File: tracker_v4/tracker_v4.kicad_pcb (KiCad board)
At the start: 2 copper layers, 62.5 x 22.1 mm, 36 parts, among them J1 USB_C_Receptacle_PowerOnly_6P, J2 P70-7000045, J3 P70-7000045, Q1 DMG9926UDM-7, U1 XIAO-ESP32-DIP, U2 LIS3DH, U3 DW01A, U4 INA226AIDGSR, U5 TP4056-42-ESOP8

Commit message: started pcb v4
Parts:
- removed J2, J3: P70-7000045, P70_7000045:HARWIN_P70-7000045
- added C4: 1u, Capacitor_SMD:C_0603_1608Metric, F.Cu at (146.0, 81.3)
- added C8: 10u, Capacitor_SMD:C_0201_0603Metric, F.Cu at (167.6, 83.7)
- added C9: 22u, Capacitor_SMD:C_1206_3216Metric, F.Cu at (166.2, 94.8)
- added D3: D, Diode_SMD:D_SOD-123F, F.Cu at (191.8, 86.7)
- added D4: D, Diode_SMD:D_SOD-123F, F.Cu at (191.8, 90.0)
- added D5: D, Diode_SMD:D_SOD-123F, F.Cu at (191.8, 93.4)
- added IC1: RT9080-33GJ5, RT9080-33GJ5:SOT94P280X100-5N, F.Cu at (166.0, 98.8)
- added R11: 10k, Resistor_SMD:R_0603_1608Metric, F.Cu at (146.0, 88.8)
- added R12: 10k, Resistor_SMD:R_0603_1608Metric, F.Cu at (146.0, 91.3)
- added R13: 4.7k, Resistor_SMD:R_0603_1608Metric, F.Cu at (146.0, 93.8)
- added SW1: SW_Push, Button_Switch_SMD:SW_Push_1P1T_NO_CK_KMR2, F.Cu at (151.3, 95.5)
- added SW2: SW_Push, Button_Switch_SMD:SW_Push_1P1T_NO_CK_KMR2, F.Cu at (151.3, 100.1)
- added U6: USBLC6-2SC6, Package_TO_SOT_SMD:SOT-23-6, F.Cu at (195.8, 82.0)
- C2: footprint Capacitor_SMD:C_0603_1608Metric -> Capacitor_SMD:C_0805_2012Metric
- J1: value USB_C_Receptacle_PowerOnly_6P -> USB_C_Receptacle_USB2.0_16P; footprint Connector_USB:USB_C_Receptacle_GCT_USB4125-xx-x-0190_6P_TopMnt_Horizontal -> Connector_USB:USB_C_Receptacle_GCT_USB4105-xx-A_16P_TopMnt_Horizontal
- R4: value 1.2k -> 3.0k
- U1: value XIAO-ESP32-DIP -> ESP32-C6-MINI-1-N4; footprint Seeed_Studio_XIAO_Series:XIAO-ESP32-C6-DIP -> ESP32-C6-MINI-1-N4:XCVR_ESP32-C6-MINI-1-N4
- moved TP7 63.2 mm to (196.0, 89.6)
- moved U5 51.0 mm to (189.0, 78.4)
- moved TP2 44.9 mm to (196.0, 86.5)
- moved C5 42.4 mm to (175.1, 86.2), turned to 0 degrees
- moved Q1 41.5 mm to (191.7, 97.4)
- moved TP8 40.5 mm to (196.0, 92.6)
- moved D1 39.6 mm to (183.1, 95.9), turned to 0 degrees
- moved J1 39.1 mm to (178.9, 80.3), turned to 0 degrees
- moved D2 37.4 mm to (183.1, 98.5), turned to 0 degrees
- moved R4 36.8 mm to (175.1, 93.8)
- moved U3 36.2 mm to (195.8, 77.4)
- moved R5 35.3 mm to (175.1, 96.3), turned to 0 degrees
- moved R8 35.3 mm to (179.1, 91.3), turned to 0 degrees
- moved R10 33.8 mm to (179.1, 96.3), turned to 0 degrees
- moved R6 33.3 mm to (179.1, 86.2), turned to 0 degrees
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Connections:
- net /Shunt_Output renamed SHUNT_OUTPUT
- C5 pad 2: GND -> Net-(D4-A)
- J1 pad B5: Net-(J1-CC2) -> USB_DM
- R5 pad 1: Net-(J1-CC2) -> USB_DM
- R5 pad 2: GND -> Net-(D3-A)
- R6 pad 2: GND -> Net-(D5-A)
- TP5 pad 1: Net-(U1-D2) -> 3v3
- U1 pad 1: Net-(U1-D0) -> GND
- U1 pad 12: 3v3 -> INA226_ALERT
- U1 pad 13: GND -> unconnected-(U1-IO1-Pad13)
- U1 pad 14: unconnected-(U1-VBUS-Pad14)_1 -> GND
- U1 pad 2: unconnected-(U1-D1-Pad2)_1 -> GND
- U1 pad 3: Net-(U1-D2) -> 3v3
- U1 pad 5: SDA -> LIS3DH_INT1
- U1 pad 6: SCL -> unconnected-(U1-IO3-Pad6)
- U2 pad 11: Net-(U1-D2) -> LIS3DH_INT1
- U4 pad 3: Net-(U1-D0) -> INA226_ALERT
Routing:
- net GND: track 153.3 -> 0.00 mm, vias 13 -> 0
- net 3v3: track 64.9 -> 0.00 mm, vias 2 -> 0
- net SHUNT_OUTPUT: track 48.4 -> 0.00 mm, vias 2 -> 0
- net /Charging_and_Battery/BAT+: track 35.4 -> 0.00 mm, vias 2 -> 0
- net USB_VBUS: track 29.2 -> 0.00 mm
- net SCL: track 26.3 -> 0.00 mm, vias 2 -> 0
- net /Charging_and_Battery/BAT-: track 21.9 -> 0.00 mm
- net SDA: track 18.2 -> 0.00 mm
- net Net-(U3-VCC): track 16.0 -> 0.00 mm, vias 2 -> 0
- net Net-(U1-D2): track 11.6 -> 0.00 mm, vias 2 -> 0
- net Net-(U1-D0): track 10.9 -> 0.00 mm
- net Net-(J1-CC2): track 9.58 -> 0.00 mm
- net Net-(U3-OD): track 7.81 -> 0.00 mm
- net Net-(U3-OC): track 7.71 -> 0.00 mm
- net /Charging_and_Battery/PROTECT_MID: track 7.67 -> 0.00 mm
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- removed copper zone on B.Cu, net GND
- removed copper zone on F.Cu, net GND
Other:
- board outline removed
- board text removed: "+"
- board text removed: "-"

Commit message: corrected schematic
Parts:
- moved U1 2.97 mm to (155.2, 83.9)
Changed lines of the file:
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@@
 	(footprint "ESP32-C6-MINI-1-N4:XCVR_ESP32-C6-MINI-1-N4"
 		(layer "F.Cu")
-		(at 155.96 86.775)
+		(at 155.2 83.9)
 		(property "Reference" "U1"
 			(at -3.325 -12.135 0)
@@
 			(polygon
 				(pts
-					(xy 149.36 75.775) (xy 162.56 75.775) (xy 162.56 81.175) (xy 149.36 81.175)
+					(xy 148.6 72.9) (xy 161.8 72.9) (xy 161.8 78.3) (xy 148.6 78.3)
 				)
 			)
@@
 			(polygon
 				(pts
-					(xy 149.36 75.775) (xy 162.56 75.775) (xy 162.56 81.175) (xy 149.36 81.175)
-				)
-			)
+					(xy 148.6 72.9) (xy 161.8 72.9) (xy 161.8 78.3) (xy 148.6 78.3)
+				)
+			)

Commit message: jk
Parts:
- removed D4, D5: D, Diode_SMD:D_SOD-123F
- added C10: 100n, Capacitor_SMD:C_0603_1608Metric, F.Cu at (124.8, 84.1)
- added C11: 10n, Capacitor_SMD:C_0603_1608Metric, F.Cu at (127.3, 84.1)
- added C12: 100n, Capacitor_SMD:C_0603_1608Metric, F.Cu at (129.8, 84.1)
- added C13: 100n, Capacitor_SMD:C_0603_1608Metric, F.Cu at (117.3, 80.1)
- added R14: 1.27M, Resistor_SMD:R_0603_1608Metric, F.Cu at (117.3, 76.1)
- added R15: 226k, Resistor_SMD:R_0603_1608Metric, F.Cu at (119.8, 76.1)
- added R16: 1M, Resistor_SMD:R_0603_1608Metric, F.Cu at (122.3, 76.1)
- added U7: TPS3899DL01DSER, TPS3899PL_footprints:DSE0006A-IPC_A, F.Cu at (142.1, 86.7)
- C8: footprint Capacitor_SMD:C_0201_0603Metric -> Capacitor_SMD:C_0805_2012Metric
- D3: value D -> SMAJ5.0A; footprint Diode_SMD:D_SOD-123F -> Diode_SMD:D_SMA
- moved C2 69.7 mm to (110.0, 119.0)
- moved U1 49.9 mm to (113.0, 110.5), turned to 90 degrees
- moved TP1 48.6 mm to (117.5, 87.7), turned to 90 degrees
- moved TP3 45.0 mm to (120.6, 87.7), turned to 90 degrees
- moved C1 44.4 mm to (120.0, 112.3), turned to 90 degrees
- moved R12 42.7 mm to (113.5, 119.0), turned to 180 degrees
- moved TP4 41.5 mm to (123.6, 87.7), turned to 90 degrees
- moved U5 41.2 mm to (149.1, 88.6), turned to 90 degrees
- moved TP2 39.1 mm to (157.2, 81.9), turned to 90 degrees
- moved U3 38.6 mm to (158.1, 86.0), turned to 90 degrees
- moved D1 38.6 mm to (147.0, 82.3), turned to 90 degrees
- moved R2 38.4 mm to (112.5, 102.5), turned to 180 degrees
- moved TP5 38.2 mm to (126.7, 87.7), turned to 90 degrees
- moved SW2 38.0 mm to (118.5, 119.3), turned to 180 degrees
- moved D2 37.3 mm to (149.6, 82.3), turned to 90 degrees
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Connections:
- C5 pad 2: Net-(D4-A) -> GND
- D3 pad 1: GND -> USB_VBUS
- D3 pad 2: Net-(D3-A) -> GND
- IC1 pad 3: SHUNT_OUTPUT -> LDO_EN
- J1 pad A6: USB_DM -> USB_DP
- J1 pad B5: USB_DM -> Net-(J1-CC2)
- J1 pad B6: USB_DM -> USB_DP
- R5 pad 1: USB_DM -> Net-(J1-CC2)
- R5 pad 2: Net-(D3-A) -> GND
- R6 pad 2: Net-(D5-A) -> GND
- R9 pad 2: /Charging_and_Battery/PROTECT_MID -> GND
- U1 pad 18: USB_DM -> USB_DP
- U6 pad 1: USB_DM -> USB_DP
- U6 pad 6: USB_DM -> USB_DP

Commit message: jk
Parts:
- moved R15 41.2 mm to (128.0, 116.5), turned to -90 degrees
- moved R14 38.8 mm to (122.5, 114.5), turned to -90 degrees
- moved C8 33.4 mm to (122.5, 111.0), turned to -90 degrees
- moved C9 33.0 mm to (130.0, 111.5)
- moved C11 32.5 mm to (125.0, 116.5), turned to -90 degrees
- moved U7 32.3 mm to (124.8, 114.0), turned to 180 degrees
- moved IC1 23.3 mm to (126.2, 110.9), turned to 0 degrees
- moved R13 12.3 mm to (120.0, 114.5), turned to -90 degrees
- moved Q1 8.47 mm to (176.0, 95.4)
- moved D3 6.31 mm to (173.5, 85.0)
- moved U6 3.28 mm to (166.0, 86.0)
- moved C1 1.50 mm to (120.0, 110.8)
- moved R11 1.50 mm to (120.0, 106.8), turned to -90 degrees

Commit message: hjk
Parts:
- moved R16 38.7 mm to (123.0, 114.8), turned to -90 degrees
- moved C4 38.3 mm to (114.0, 121.5), turned to 180 degrees
- moved C3 37.2 mm to (129.5, 120.0), turned to 180 degrees
- moved C13 36.6 mm to (128.2, 115.0), turned to 0 degrees
- moved Q1 35.4 mm to (142.5, 106.6), turned to 0 degrees
- moved TP5 33.9 mm to (126.0, 121.5)
- moved TP1 31.8 mm to (123.0, 119.0)
- moved TP8 30.0 mm to (139.0, 99.5)
- moved C12 29.4 mm to (128.3, 113.5), turned to 0 degrees
- moved D1 27.8 mm to (147.1, 110.2)
- moved D2 27.8 mm to (149.7, 110.2)
- moved U5 26.9 mm to (148.1, 115.5)
- moved BT1 25.8 mm to (135.5, 106.0), turned to 0 degrees
- moved D3 25.1 mm to (161.7, 107.2), turned to -90 degrees
- moved U6 24.9 mm to (155.7, 108.7)
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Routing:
- net GND: track 0.00 -> 242.6 mm, vias 0 -> 22
- net 3v3: track 0.00 -> 89.0 mm, vias 0 -> 9
- net USB_DM: track 0.00 -> 58.8 mm, vias 0 -> 7
- net USB_VBUS: track 0.00 -> 56.2 mm, vias 0 -> 5
- net USB_DP: track 0.00 -> 55.1 mm, vias 0 -> 6
- net /Charging_and_Battery/BAT+: track 0.00 -> 51.2 mm, vias 0 -> 4
- net SCL: track 0.00 -> 50.1 mm, vias 0 -> 3
- net SDA: track 0.00 -> 49.3 mm, vias 0 -> 4
- net INA226_ALERT: track 0.00 -> 31.3 mm, vias 0 -> 2
- net SHUNT_OUTPUT: track 0.00 -> 30.8 mm
- net LIS3DH_INT1: track 0.00 -> 21.8 mm, vias 0 -> 2
- net Net-(U1-EN): track 0.00 -> 11.8 mm
- net UVLO_SENSE: track 0.00 -> 10.7 mm
- net LDO_EN: track 0.00 -> 9.22 mm, vias 0 -> 2
- net /Charging_and_Battery/BAT-: track 0.00 -> 8.31 mm
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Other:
- board outline added: 63 x 25.4 mm

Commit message: done
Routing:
- net GND: track 242.6 -> 250.7 mm, vias 22 -> 25
- net /Charging_and_Battery/BAT+: track 51.2 -> 48.5 mm
- added copper zone on B.Cu, net GND
- added copper zone on F.Cu, net GND

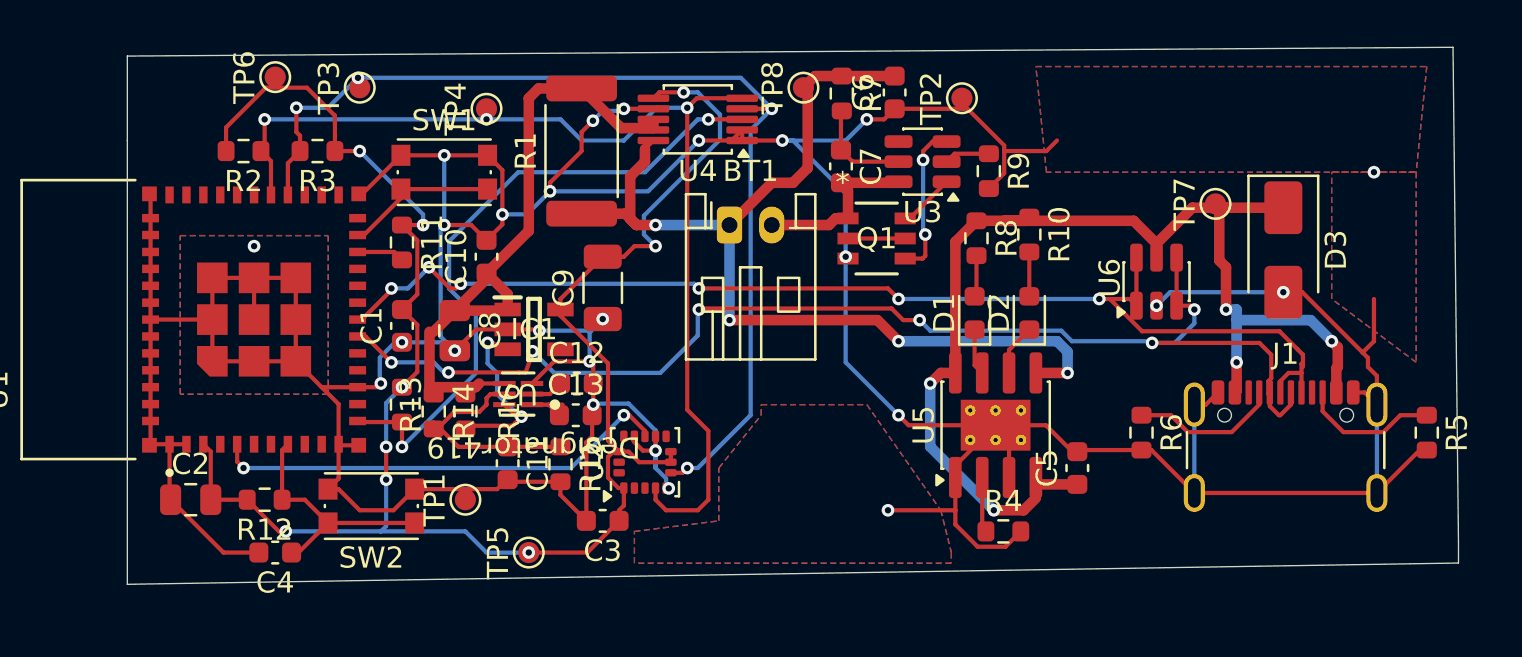
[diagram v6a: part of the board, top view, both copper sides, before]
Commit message: added vias and ground plane everywhere
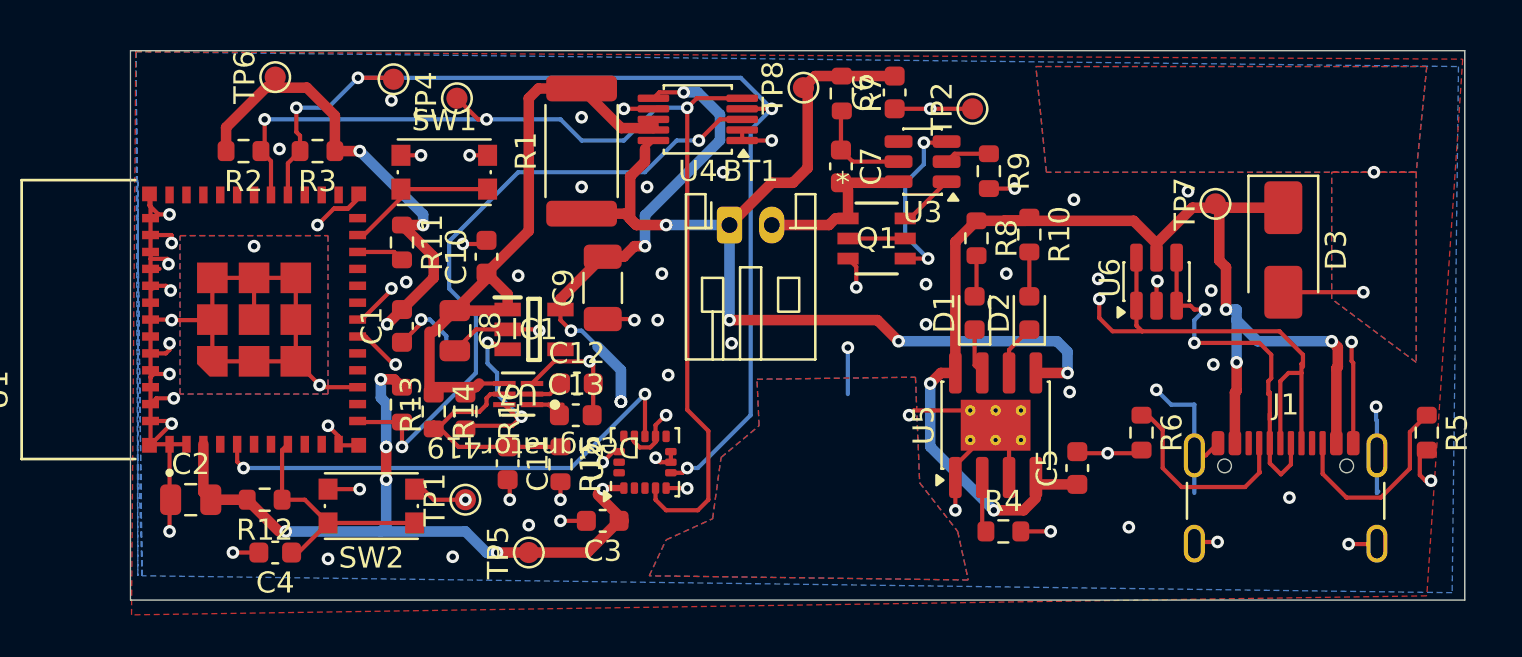
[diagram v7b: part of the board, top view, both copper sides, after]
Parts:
- moved J1 2.40 mm to (161.8, 120.0)
- moved TP3 1.65 mm to (119.6, 99.1)
- moved TP4 1.49 mm to (122.6, 100.0)
- moved TP2 0.71 mm to (147.0, 100.5)
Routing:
- net GND: track 250.7 -> 144.4 mm, vias 25 -> 74
- net USB_VBUS: track 56.2 -> 61.0 mm
- net USB_DP: track 55.1 -> 59.3 mm, vias 6 -> 2
- net 3v3: track 89.0 -> 93.2 mm, vias 9 -> 16
- net Net-(J1-CC2): track 6.56 -> 9.47 mm
- net Net-(J1-CC1): track 7.01 -> 9.74 mm
- net LIS3DH_INT1: track 21.8 -> 23.7 mm
- net SCL: track 50.1 -> 51.9 mm
- net SDA: track 49.3 -> 51.1 mm
- net Net-(U3-OC): track 7.31 -> 8.48 mm
- net USB_DM: track 58.8 -> 59.3 mm, vias 7 -> 3
- added copper zone on In1.Cu, net GND
- added copper zone on In2.Cu, net GND
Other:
- board size 63 x 25.4 mm -> 63.2 x 26 mm
- copper layers 2 -> 4

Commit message: jkd
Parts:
- renumbered SW1 to BOOT, SW2 to RESET
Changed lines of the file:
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@@
 		(capping no)
 		(filling no)
-		(zone_defaults)
 		(pcbplotparams
 			(layerselection 0x00000000_00000000_55555555_5755f5ff)
@@
 		(descr "CK components KMR2 tactile switch http://www.ckswitches.com/media/1479/kmr2.pdf")
 		(tags "tactile switch kmr2")
-		(property "Reference" "SW1"
+		(property "Reference" "BOOT"
 			(at 0 -2.45 0)
 			(layer "F.SilkS")
@@
 		(descr "CK components KMR2 tactile switch http://www.ckswitches.com/media/1479/kmr2.pdf")
 		(tags "tactile switch kmr2")
-		(property "Reference" "SW2"
+		(property "Reference" "RESET"
 			(at 0 -2.45 0)
 			(layer "F.SilkS")
